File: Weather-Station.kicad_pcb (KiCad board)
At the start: 2 copper layers, 125 x 125 mm, 64 parts, among them IC1 TPS3700DDCR, J1 PV IN, J2 Screw_Terminal_01x12, J3 PDB-C139, J4 TMP36GT9Z, J5 Lightning Sensor, J6 RG-15 Rain Sensor, J7 BME280 Sensor, U1 MCP73812T-420I-OT, U2 TDC1000PW, U3 SiT8918AE-13-33E-5.000000G, U4 TPS73633DBV, U5 TDC7200PW, U6 Wemos_S2, U7 ADS1115IDGS

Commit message: Continued board layout
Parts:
- moved R13 197.2 mm to (77.0, 87.9)
- moved R6 195.6 mm to (77.1, 95.9)
- moved C2 179.5 mm to (106.9, 52.0), turned to 180 degrees
- moved R5 176.7 mm to (70.7, 47.0), turned to 90 degrees
- moved R2 169.2 mm to (74.2, 56.6)
- moved R3 164.7 mm to (74.3, 60.3)
- moved R12 162.4 mm to (73.0, 87.9)
- moved R1 158.8 mm to (74.2, 52.8)
- moved U2 158.5 mm to (68.5, 94.3)
- moved R15 157.3 mm to (80.7, 53.5)
- moved R7 156.9 mm to (86.5, 52.2), turned to 180 degrees
- moved R18 155.9 mm to (90.7, 58.7), turned to 90 degrees
- moved R19 154.4 mm to (90.6, 54.4), turned to 90 degrees
- moved C1 151.6 mm to (96.7, 52.3), turned to 180 degrees
- moved R14 148.5 mm to (80.9, 94.7)
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
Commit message: Continued board layout
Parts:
- moved C8 60.3 mm to (120.6, 56.9)
- moved C9 60.3 mm to (128.8, 59.3)
- moved R12 60.3 mm to (124.7, 56.9)
- moved R13 60.3 mm to (128.7, 56.9)
- moved R14 60.3 mm to (132.7, 63.7)
- moved R4 60.3 mm to (132.7, 65.7)
- moved R6 60.3 mm to (128.8, 64.9)
- moved U2 60.3 mm to (120.2, 63.4)
- moved U5 60.1 mm to (104.0, 61.7)
- moved C11 26.5 mm to (73.9, 52.8)
- moved C14 26.5 mm to (78.5, 52.1)
- moved C15 26.5 mm to (82.5, 52.4)
- moved C16 26.5 mm to (82.4, 56.3)
- moved U4 26.5 mm to (78.3, 55.7)
- moved U6 22.2 mm to (116.2, 134.2)
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
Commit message: more pcb layout
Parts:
- removed IC1: TPS3700DDCR, Package_TO_SOT_SMD:TSOT-23-6
- removed the U4 at (78.3, 55.7)
- removed the U6 at (116.2, 134.2)
- added J3: TX2, TerminalBlock:TerminalBlock_bornier-2_P5.08mm, F.Cu at (110.4, 51.8)
- added J4: RX1, TerminalBlock:TerminalBlock_bornier-2_P5.08mm, F.Cu at (122.2, 55.8)
- added J5: RX2, TerminalBlock:TerminalBlock_bornier-2_P5.08mm, F.Cu at (132.6, 60.2)
- added J6: RTD1, TerminalBlock:TerminalBlock_bornier-2_P5.08mm, F.Cu at (139.1, 69.6)
- added J7: RTD2, TerminalBlock:TerminalBlock_bornier-2_P5.08mm, F.Cu at (144.0, 79.6)
- added U2: TPS3700DDCR, Package_TO_SOT_SMD:TSOT-23-6, F.Cu at (62.2, 107.3)
- added U5: TPS73633DBV, Package_TO_SOT_SMD:SOT-23-5, F.Cu at (64.0, 74.2)
- added U7: Wemos_S2, ESP32:WEMOS_S2, F.Cu at (107.2, 135.5)
- J2: value Screw_Terminal_01x12 -> TX1; footprint TerminalBlock_Phoenix:TerminalBlock_Phoenix_MKDS-1,5-12-5.08_1x12_P5.08mm_Horizontal -> TerminalBlock:TerminalBlock_bornier-2_P5.08mm
- moved R29 199.5 mm to (86.2, 61.5), turned to 195 degrees
- moved J9 194.0 mm to (76.2, 60.5), turned to 217 degrees
- moved R16 172.4 mm to (77.5, 32.8), turned to 180 degrees
- moved C19 157.6 mm to (73.9, 70.8), turned to 217 degrees
- moved R9 153.1 mm to (96.8, 30.5)
- moved U8 126.3 mm to (78.9, 67.0), turned to 217 degrees
- moved R23 111.5 mm to (207.5, 20.0)
- moved C9 103.3 mm to (229.5, 82.3)
- moved J11 99.7 mm to (64.5, 114.2), turned to 308 degrees
- moved J10 99.5 mm to (134.2, 122.5), turned to 57 degrees
- moved C17 98.9 mm to (202.5, 28.5)
- moved U6 95.5 mm to (193.5, 28.5)
- moved R22 94.3 mm to (201.8, 36.1)
- moved R8 93.6 mm to (59.0, 79.8), turned to 0 degrees
- moved J1 92.8 mm to (59.8, 92.0), turned to 270 degrees
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- renumbered J5 to J10, J6 to J11, J7 to J12, J3 to J8, J4 to J9, U2 to U3, U3 to U4, U5 to U6, U7 to U8
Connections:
- R5 pad 1: TX1 -> TX2
- R5 pad 2: Net-(J2-Pad1) -> Net-(J3-Pad1)
- R7 pad 1: TX2 -> TX1
- R7 pad 2: Net-(J2-Pad3) -> Net-(J2-Pad1)
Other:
- board size 125 x 125 mm -> 100 x 100 mm
- board text added: "+"
- board text added: "-"
- board text added: "BME280"
- board text added: "LIGHTNING"
- board text added: "PDB"
- board text added: "PV IN"
- board text added: "RG15"
- board text added: "RX"
- board text added: "RX1"
- board text added: "RX2"
- board text added: "SCL"
- board text added: "SDA"
- board text added: "TMP36"
- board text added: "TX"
- board text added: "TX1"
- board text added: "TX2"

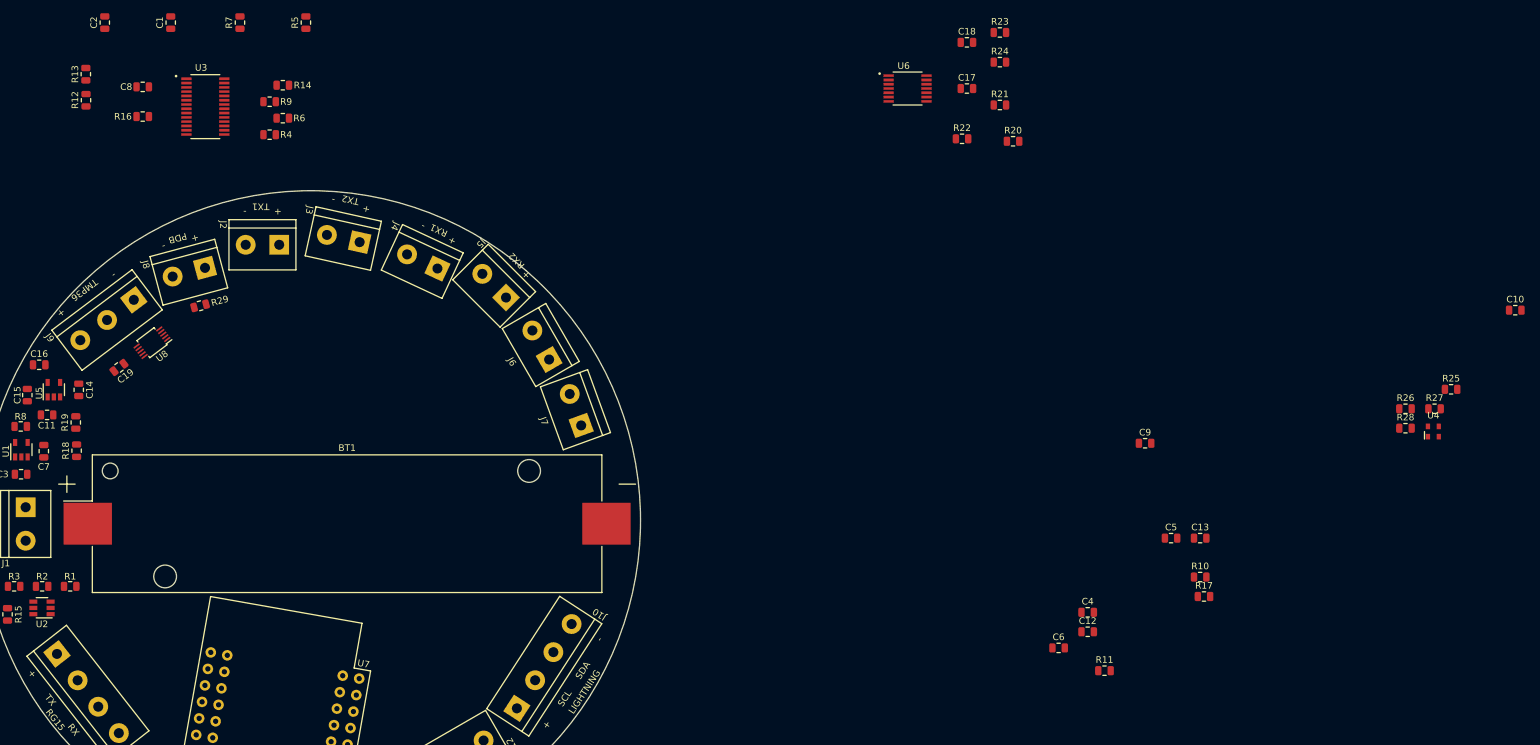
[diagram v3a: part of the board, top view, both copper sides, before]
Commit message: PCB component placement complete.
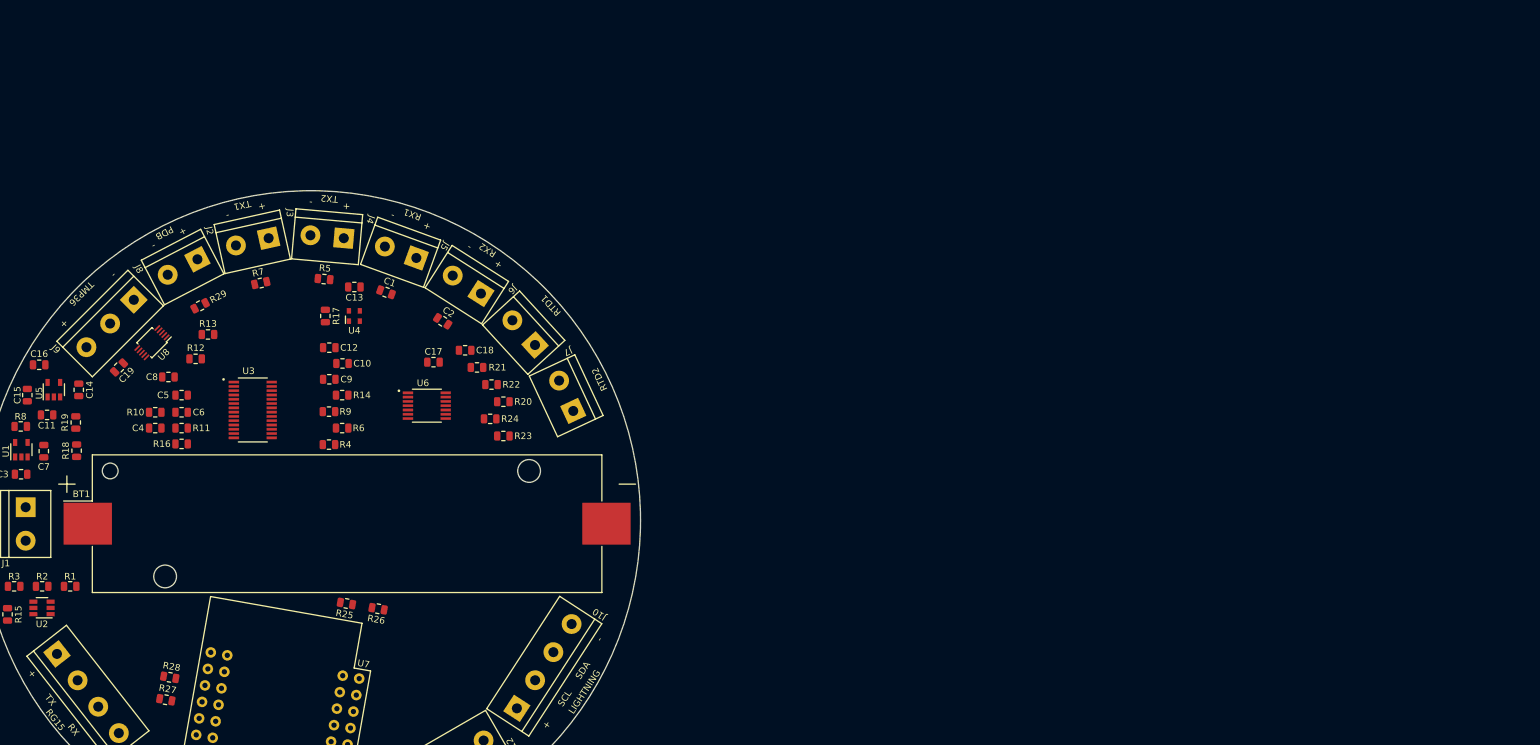
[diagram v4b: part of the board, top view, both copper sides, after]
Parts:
- moved R27 197.4 mm to (81.0, 121.2), turned to 350 degrees
- moved R28 191.2 mm to (81.6, 117.8), turned to 350 degrees
- moved C10 178.0 mm to (107.8, 70.2)
- moved R25 170.7 mm to (108.4, 106.6), turned to 170 degrees
- moved U4 164.6 mm to (109.6, 63.0)
- moved R10 160.4 mm to (79.4, 77.6), turned to 180 degrees
- moved R26 158.7 mm to (113.2, 107.4), turned to 170 degrees
- moved C5 151.6 mm to (83.4, 75.0), turned to 180 degrees
- moved R11 144.7 mm to (83.4, 80.0), turned to 180 degrees
- moved C4 144.1 mm to (79.4, 80.0)
- moved R17 139.9 mm to (105.2, 63.0), turned to 270 degrees
- moved C6 137.7 mm to (83.4, 77.6), turned to 180 degrees
- moved C13 133.8 mm to (109.6, 58.6)
- moved C9 124.1 mm to (105.8, 72.6)
- moved C12 122.8 mm to (105.8, 67.8)
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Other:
- board text added: "RTD1"
- board text added: "RTD2"

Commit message: to be continued
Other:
- outline, holes or cut-outs redrawn
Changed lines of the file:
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@@
   (general
     (thickness 1.6)
-    (drawings 39)
+    (drawings 40)
     (tracks 0)
     (zones 0)
@@
     )
   )
+  (gr_arc (start 103 94) (end 152.999599 94.199997) (angle -180.2291814) (layer Edge.Cuts) (width 0.05))
+  (gr_arc (start 103 94) (end 53 94) (angle -179.7708181) (layer Edge.Cuts) (width 0.05))
   (gr_text RTD2 (at 146.8 72.6 115) (layer F.SilkS)
     (effects (font (size 1 1) (thickness 0.15)))
@@
     (effects (font (size 1 1) (thickness 0.15)))
   )
-  (gr_text "PV IN" (at 53.75 94.5 270) (layer F.SilkS)
-    (effects (font (size 1 1) (thickness 0.15)))
-  )
-  (gr_text - (at 54.75 97 90) (layer F.SilkS)
-    (effects (font (size 1 1) (thickness 0.15)))
-  )
-  (gr_text + (at 54.75 92 90) (layer F.SilkS)
-    (effects (font (size 1 1) (thickness 0.15)))
-  )
-  (gr_circle (center 103 94) (end 153 94) (layer Edge.Cuts) (width 0.05))
+  (gr_text "PV IN" (at 53.8 94.5 270) (layer F.SilkS)
+    (effects (font (size 1 1) (thickness 0.15)))
+  )
+  (gr_text - (at 54.8 97.2 90) (layer F.SilkS)
+    (effects (font (size 1 1) (thickness 0.15)))
+  )
+  (gr_text + (at 55 92 90) (layer F.SilkS)
+    (effects (font (size 1 1) (thickness 0.15)))
+  )
 )

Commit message: pcb routing work continues
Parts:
- added TP1: TestPoint, TestPoint:TestPoint_Keystone_5000-5004_Miniature, F.Cu at (69.0, 108.2)
- added TP2: TestPoint, TestPoint:TestPoint_Keystone_5000-5004_Miniature, F.Cu at (114.5, 61.0)
- moved R7 7.01 mm to (102.4, 57.6), turned to 90 degrees
- moved C1 6.45 mm to (120.5, 61.5), turned to 90 degrees
- moved C16 3.51 mm to (65.3, 70.1)
- moved C10 2.00 mm to (105.8, 70.2)
- moved C2 1.57 mm to (121.6, 64.5), turned to 0 degrees
- moved R19 1.26 mm to (67.5, 80.4)
- moved C7 1.20 mm to (62.5, 84.7)
- moved R18 1.20 mm to (67.5, 84.6)
- moved R26 1.08 mm to (112.6, 106.5), turned to 0 degrees
- moved C19 0.85 mm to (74.7, 70.5), turned to 135 degrees
- moved C11 0.81 mm to (63.7, 78.4)
- moved C18 0.80 mm to (127.2, 68.2)
- moved R22 0.50 mm to (130.9, 73.4)
- moved R5 0.45 mm to (105.4, 57.6), turned to 90 degrees
- moved C3 0.40 mm to (59.0, 87.4)
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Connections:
- U7 pad 32: Net-(U7-Pad32) -> TDC1000CHSEL
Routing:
- net +3V3: track 0.00 -> 167.4 mm, vias 0 -> 4
- net +BATT: track 0.00 -> 136.2 mm, vias 0 -> 4
- net SCK: track 0.00 -> 112.6 mm, vias 0 -> 3
- net MOSI: track 0.00 -> 101.6 mm, vias 0 -> 2
- net MISO: track 0.00 -> 93.5 mm, vias 0 -> 3
- net TDC1000CHSEL: track 0.00 -> 69.3 mm, vias 0 -> 1
- net SDA: track 0.00 -> 61.0 mm
- net RTD2: track 0.00 -> 60.6 mm, vias 0 -> 1
- net RTD1: track 0.00 -> 59.9 mm, vias 0 -> 1
- net BATTOK: track 0.00 -> 58.0 mm
- net SCL: track 0.00 -> 57.3 mm
- net TDC1000EN: track 0.00 -> 54.7 mm, vias 0 -> 1
- net ERRB: track 0.00 -> 50.4 mm
- net TDC1000RESET: track 0.00 -> 49.8 mm, vias 0 -> 1
- net CLK: track 0.00 -> 47.5 mm
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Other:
- net class RX added: clearance 0.2, trace_width 0.25, via_dia 0.8, via_drill 0.4
- net class TX added: clearance 0.2, trace_width 0.25, via_dia 0.8, via_drill 0.4

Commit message: Routing completed.
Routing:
- net +3V3: track 167.4 -> 341.8 mm, vias 4 -> 9
- net TDC7200CSB: track 11.9 -> 95.7 mm, vias 1 -> 3
- net SCL: track 57.3 -> 123.7 mm, vias 0 -> 3
- net SDA: track 61.0 -> 127.0 mm, vias 0 -> 2
- net TDC1000CSB: track 4.08 -> 61.8 mm, vias 1 -> 3
- net TX: track 0.00 -> 49.8 mm
- net TDC7200INT: track 22.3 -> 70.6 mm, vias 0 -> 2
- net RX: track 0.00 -> 46.2 mm
- net TDC7200EN: track 12.9 -> 55.4 mm
- net GND: track 0.00 -> 20.3 mm, vias 1 -> 7
- net ERRB: track 50.4 -> 68.3 mm, vias 0 -> 1
- net Net-(C14-Pad1): track 4.80 -> 2.70 mm
- net TDC1000RESET: track 49.8 -> 48.3 mm
- added copper zone on B.Cu, net GND
- added copper zone on F.Cu, net GND
